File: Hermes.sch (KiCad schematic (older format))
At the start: 1 part

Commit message: Adding Hermes 2 schematic files.
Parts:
- added D1: LED_Debug0, symbol LED
- added D2: LED_Debug1, symbol LED
- added D3: LED_Debug2, symbol LED
- added R2, R3: 120Ω, symbol R
- added U1: Teensy3.2, symbol Teensy3.2
- R1: value 10kΩ -> 120Ω; footprint Footprints:R_CMS1206 -> (none)
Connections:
- net labels added: +3.3V, CAN_RX, CAN_TX, DIAG_1, DIAG_2, ENC_1_A, ENC_1_B, ENC_2_A, ENC_2_B, GP2_1_Signal, GP2_2_Signal, GP2_3_Signal, GP2_4_Signal, GP2_5_Signal, GP2_6_Signal, IN_A_1, IN_A_2, IN_B_1, IN_B_2, LED_Debug0, LED_Debug1, LED_Debug2, LimitSwitch_1_Signal, LimitSwitch_2_Signal, LimitSwitch_3_Signal, LimitSwitch_4_Signal, PWM_1, PWM_2, PullSignal, SCL, SDA, UART0_RX, UART0_TX, UART1_RX, UART1_TX
- wire segments 106 -> 115

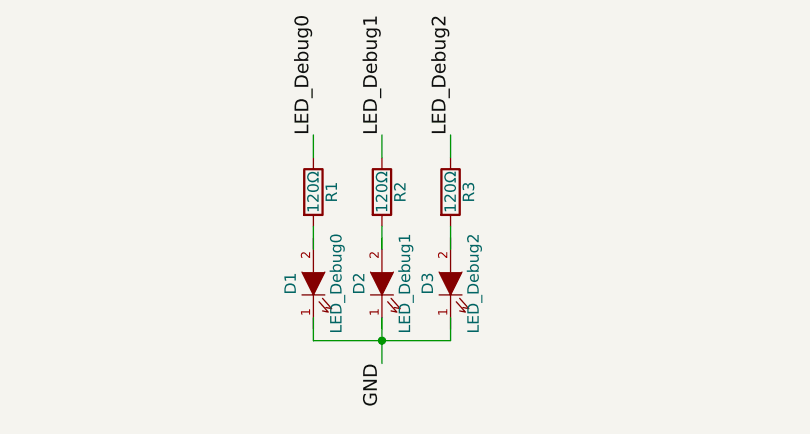
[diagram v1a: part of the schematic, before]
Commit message: Changing some value fields on the schematics for a better grouped_csv BOM generation.
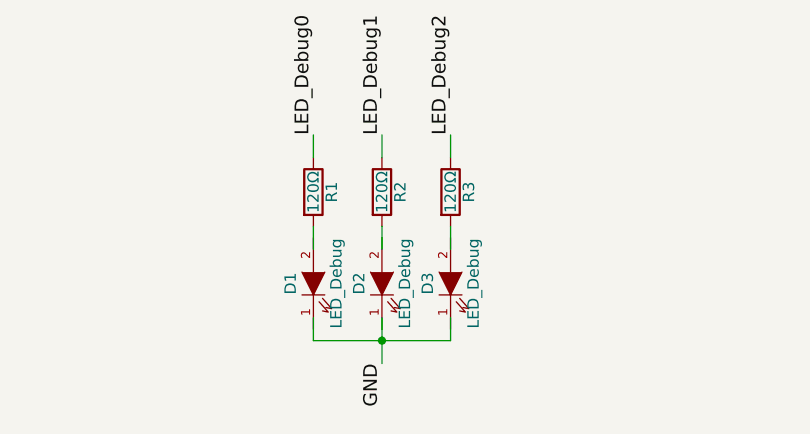
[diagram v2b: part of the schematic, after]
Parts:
- D1: value LED_Debug0 -> LED_Debug
- D2: value LED_Debug1 -> LED_Debug
- D3: value LED_Debug2 -> LED_Debug
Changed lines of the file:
@@
 P 5550 6900
 F 0 "D1" H 5550 7000 50  0000 C CNN
-F 1 "LED_Debug0" H 5550 6800 50  0000 C CNN
+F 1 "LED_Debug" H 5550 6800 50  0000 C CNN
 F 2 "" H 5550 6900 50  0001 C CNN
 F 3 "" H 5550 6900 50  0001 C CNN
@@
 P 5850 6900
 F 0 "D2" H 5850 7000 50  0000 C CNN
-F 1 "LED_Debug1" H 5850 6800 50  0000 C CNN
+F 1 "LED_Debug" H 5850 6800 50  0000 C CNN
 F 2 "" H 5850 6900 50  0001 C CNN
 F 3 "" H 5850 6900 50  0001 C CNN
@@
 P 6150 6900
 F 0 "D3" H 6150 7000 50  0000 C CNN
-F 1 "LED_Debug2" H 6150 6800 50  0000 C CNN
+F 1 "LED_Debug" H 6150 6800 50  0000 C CNN
 F 2 "" H 6150 6900 50  0001 C CNN
 F 3 "" H 6150 6900 50  0001 C CNN

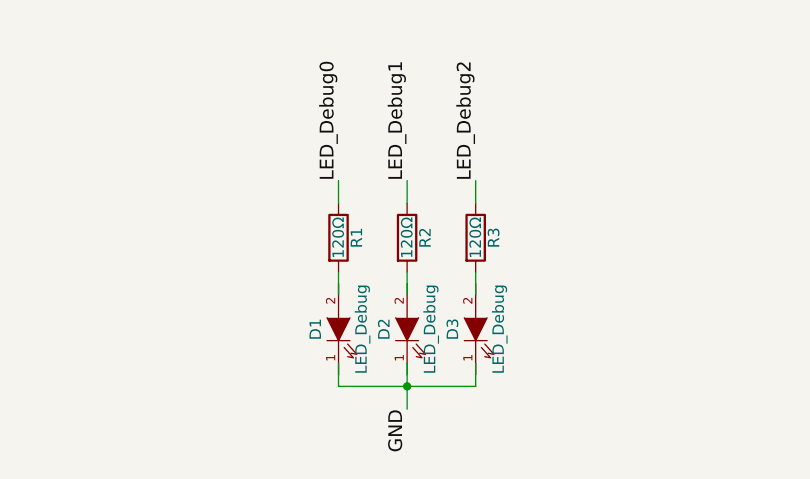
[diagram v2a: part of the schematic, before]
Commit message: Updating the schematic's annotations.
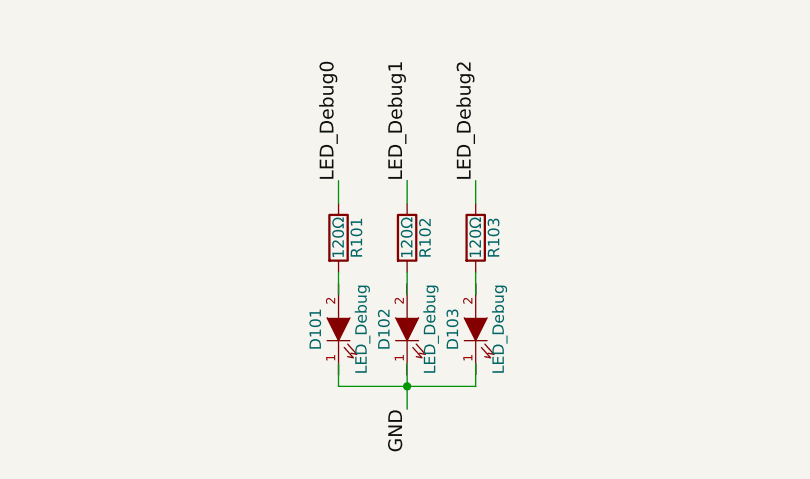
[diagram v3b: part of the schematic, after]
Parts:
- renumbered D1 to D101, D2 to D102, D3 to D103, R1 to R101, R2 to R102, R3 to R103, U1 to U101
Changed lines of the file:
@@
 GND
 $Comp
-L Teensy3.2 U1
+L Teensy3.2 U101
 U 1 1 59FF5AE8
 P 5850 3800
-F 0 "U1" H 5850 5300 60  0000 C CNN
+F 0 "U101" H 5850 5300 60  0000 C CNN
 F 1 "Teensy3.2" H 5850 2300 60  0000 C CNN
 F 2 "" H 5850 3000 60  0000 C CNN
@@
 SCL
 $Comp
-L LED D1
+L LED D101
 U 1 1 5A01F75F
 P 5550 6900
-F 0 "D1" H 5550 7000 50  0000 C CNN
+F 0 "D101" H 5550 7000 50  0000 C CNN
 F 1 "LED_Debug" H 5550 6800 50  0000 C CNN
 F 2 "" H 5550 6900 50  0001 C CNN
@@
 $EndComp
 $Comp
-L LED D2
+L LED D102
 U 1 1 5A01FF7D
 P 5850 6900
-F 0 "D2" H 5850 7000 50  0000 C CNN
+F 0 "D102" H 5850 7000 50  0000 C CNN
 F 1 "LED_Debug" H 5850 6800 50  0000 C CNN
 F 2 "" H 5850 6900 50  0001 C CNN
@@
 $EndComp
 $Comp
-L LED D3
+L LED D103
 U 1 1 5A020505
 P 6150 6900
-F 0 "D3" H 6150 7000 50  0000 C CNN
+F 0 "D103" H 6150 7000 50  0000 C CNN
 F 1 "LED_Debug" H 6150 6800 50  0000 C CNN
 F 2 "" H 6150 6900 50  0001 C CNN
@@
 $EndComp
 $Comp
-L R R1
+L R R101
 U 1 1 5A0213BF
 P 5550 6500
-F 0 "R1" V 5630 6500 50  0000 C CNN
+F 0 "R101" V 5630 6500 50  0000 C CNN
 F 1 "120Ω" V 5550 6500 50  0000 C CNN
 F 2 "" V 5480 6500 50  0001 C CNN
@@
 $EndComp
 $Comp
-L R R2
+L R R102
 U 1 1 5A025419
 P 5850 6500
-F 0 "R2" V 5930 6500 50  0000 C CNN
+F 0 "R102" V 5930 6500 50  0000 C CNN
 F 1 "120Ω" V 5850 6500 50  0000 C CNN
 F 2 "" V 5780 6500 50  0001 C CNN
@@
 $EndComp
 $Comp
-L R R3
+L R R103
 U 1 1 5A0255F2
 P 6150 6500
-F 0 "R3" V 6230 6500 50  0000 C CNN
+F 0 "R103" V 6230 6500 50  0000 C CNN
 F 1 "120Ω" V 6150 6500 50  0000 C CNN
 F 2 "" V 6080 6500 50  0001 C CNN

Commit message: Setting the schematic's footprints.
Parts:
- D101, D102, D103: footprint (none) -> LEDs:LED_1206_HandSoldering
- R101, R102, R103: footprint (none) -> Resistors_SMD:R_1206_HandSoldering
- U101: footprint (none) -> xenocad.teensy:Teensy30_31_32_LC_sides_bottom
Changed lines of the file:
@@
 F 0 "U101" H 5850 5300 60  0000 C CNN
 F 1 "Teensy3.2" H 5850 2300 60  0000 C CNN
-F 2 "" H 5850 3000 60  0000 C CNN
+F 2 "xenocad.teensy:Teensy30_31_32_LC_sides_bottom" H 5850 3000 60  0001 C CNN
 F 3 "" H 5850 3000 60  0000 C CNN
 	1    5850 3800
@@
 F 0 "D101" H 5550 7000 50  0000 C CNN
 F 1 "LED_Debug" H 5550 6800 50  0000 C CNN
-F 2 "" H 5550 6900 50  0001 C CNN
+F 2 "LEDs:LED_1206_HandSoldering" H 5550 6900 50  0001 C CNN
 F 3 "" H 5550 6900 50  0001 C CNN
 	1    5550 6900
@@
 F 0 "D102" H 5850 7000 50  0000 C CNN
 F 1 "LED_Debug" H 5850 6800 50  0000 C CNN
-F 2 "" H 5850 6900 50  0001 C CNN
+F 2 "LEDs:LED_1206_HandSoldering" H 5850 6900 50  0001 C CNN
 F 3 "" H 5850 6900 50  0001 C CNN
 	1    5850 6900
@@
 F 0 "D103" H 6150 7000 50  0000 C CNN
 F 1 "LED_Debug" H 6150 6800 50  0000 C CNN
-F 2 "" H 6150 6900 50  0001 C CNN
+F 2 "LEDs:LED_1206_HandSoldering" H 6150 6900 50  0001 C CNN
 F 3 "" H 6150 6900 50  0001 C CNN
 	1    6150 6900
@@
 F 0 "R101" V 5630 6500 50  0000 C CNN
 F 1 "120Ω" V 5550 6500 50  0000 C CNN
-F 2 "" V 5480 6500 50  0001 C CNN
+F 2 "Resistors_SMD:R_1206_HandSoldering" V 5480 6500 50  0001 C CNN
 F 3 "" H 5550 6500 50  0001 C CNN
 	1    5550 6500
@@
 F 0 "R102" V 5930 6500 50  0000 C CNN
 F 1 "120Ω" V 5850 6500 50  0000 C CNN
-F 2 "" V 5780 6500 50  0001 C CNN
+F 2 "Resistors_SMD:R_1206_HandSoldering" V 5780 6500 50  0001 C CNN
 F 3 "" H 5850 6500 50  0001 C CNN
 	1    5850 6500
@@
 F 0 "R103" V 6230 6500 50  0000 C CNN
 F 1 "120Ω" V 6150 6500 50  0000 C CNN
-F 2 "" V 6080 6500 50  0001 C CNN
+F 2 "Resistors_SMD:R_1206_HandSoldering" V 6080 6500 50  0001 C CNN
 F 3 "" H 6150 6500 50  0001 C CNN
 	1    6150 6500
